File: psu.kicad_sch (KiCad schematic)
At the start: 9 parts, among them T1 Transformer_1P_2S, U2 PC817, U3 TL431DBZ

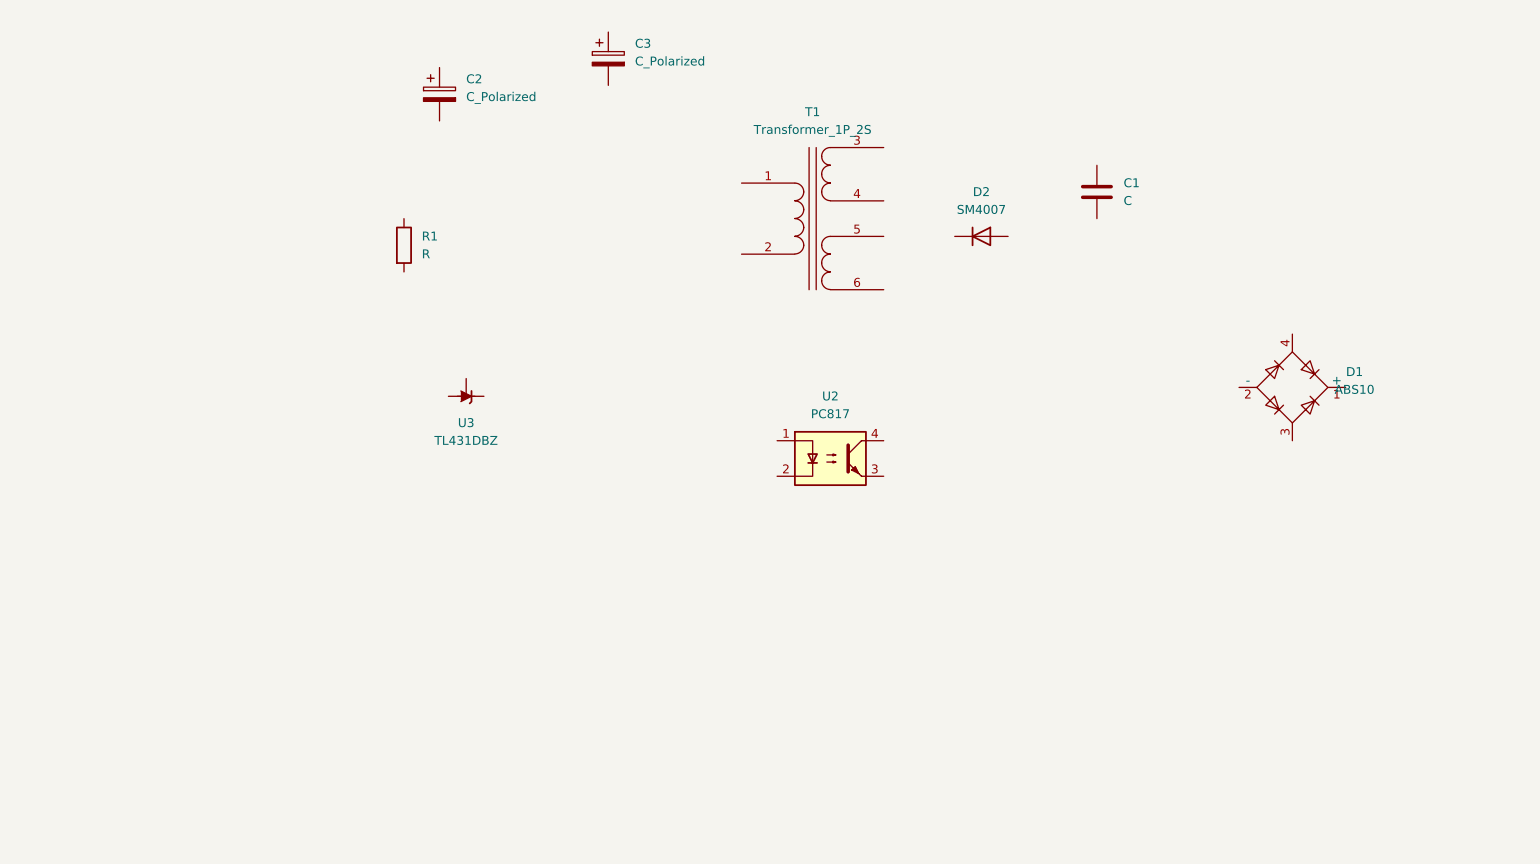
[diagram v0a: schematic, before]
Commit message: progress in psu section:footprints added:flyback ic yet to be added
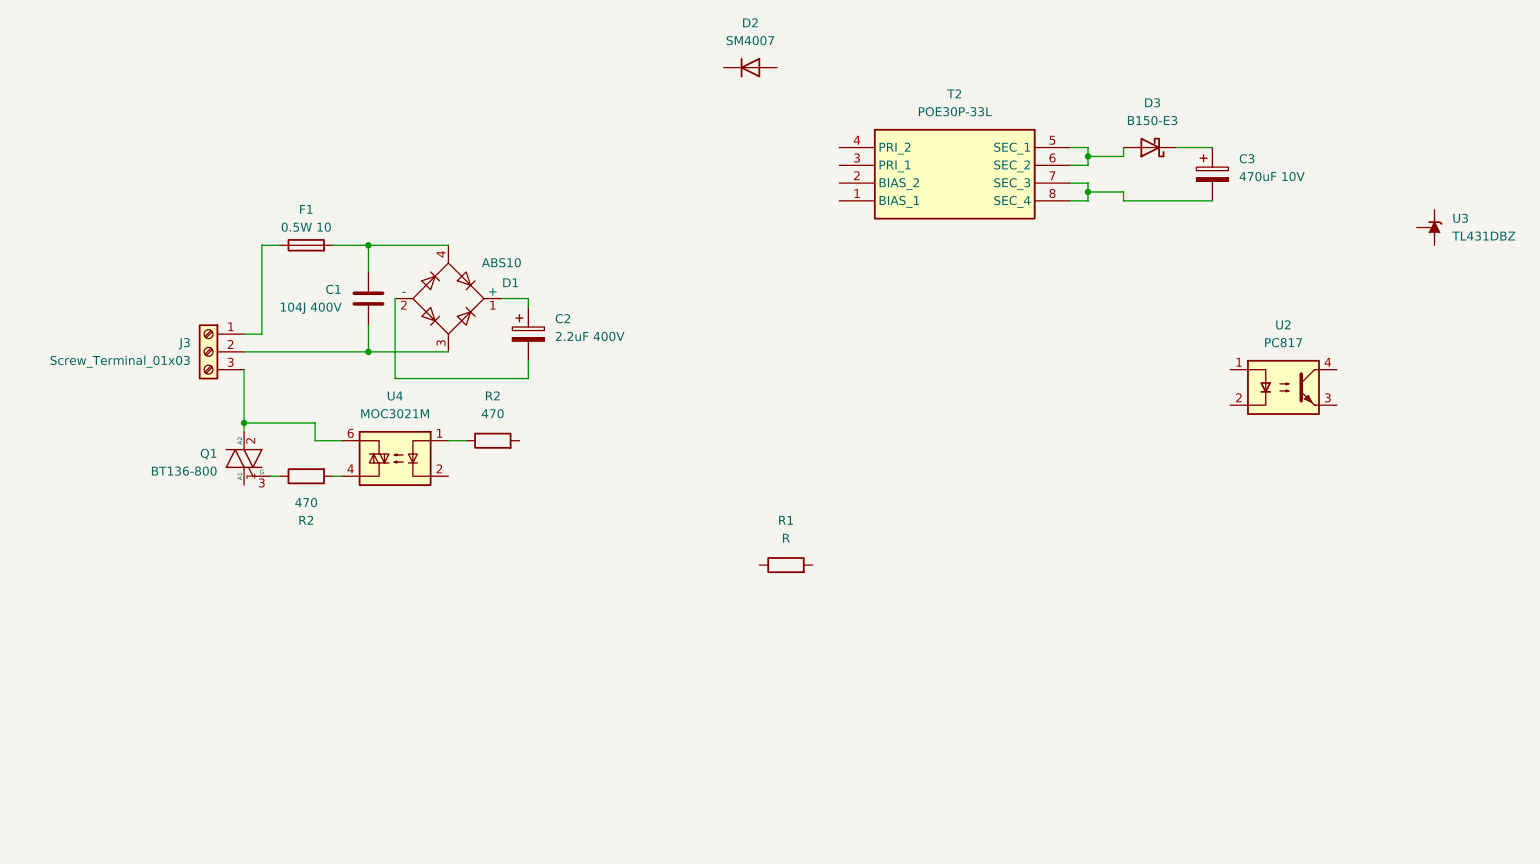
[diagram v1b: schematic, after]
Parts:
- removed T1: Transformer_1P_2S, symbol Device:Transformer_1P_2S
- added D3: B150-E3, Diode_SMD:D_SMA, symbol Diode:B150-E3
- added F1: 0.5W 10, Resistor_THT:R_Axial_DIN0411_L9.9mm_D3.6mm_P15.24mm_Horizontal, symbol Device:Fuse
- added J3: Screw_Terminal_01x03, TerminalBlock_Phoenix:TerminalBlock_Phoenix_MKDS-1,5-3-5.08_1x03_P5.08mm_Horizontal, symbol Connector:Screw_Terminal_01x03
- added Q1: BT136-800, Package_TO_SOT_THT:TO-220-3_Vertical, symbol Triac_Thyristor:BT136-800
- added R2 (x2): 470, Resistor_SMD:R_1206_3216Metric, symbol Device:R
- added T2: POE30P-33L, footprint:POE30P33L, symbol POE30P-33L:POE30P-33L
- added U4: MOC3021M, Package_DIP:DIP-6_W8.89mm_SMDSocket_LongPads, symbol Relay_SolidState:MOC3021M
- C1: value C -> 104J 400V; footprint (none) -> Capacitor_THT:C_Rect_L10.3mm_W4.5mm_P7.50mm_MKS4
- C2: value C_Polarized -> 2.2uF 400V; footprint (none) -> Capacitor_THT:CP_Radial_D8.0mm_P3.50mm
- C3: value C_Polarized -> 470uF 10V
- U2: footprint Package_DIP:DIP-4_W7.62mm -> Package_DIP:DIP-4_W7.62mm_SMDSocket_SmallPads
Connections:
- net at D1.1 (+): now also C2.1
- net at D1.2 (-): now also C2.2
- net at D1.3: now also C1.2, J3.2 (Pin_2)
- net at D1.4: now also C1.1, F1.2
- net at C3.1: now also D3.1 (K)
- net at C3.2: now also T2.7 (SEC_3), T2.8 (SEC_4)
- new net: D3.2 (A), T2.5 (SEC_1), T2.6 (SEC_2)
- new net: F1.1, J3.1 (Pin_1)
- new net: R2.1, U4.1
- new net: R2.2, U4.4
- new net: J3.3 (Pin_3), Q1.2 (A2), U4.6
- new net: Q1.3 (G), R2.1
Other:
- moved on the sheet: C1, C2, C3, D1, D2, R1, U2, U3

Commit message: viper22as, transformer, hierarchical connections
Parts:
- added U5: VIPer22AS, Package_SO:SOIC-8_3.9x4.9mm_P1.27mm, symbol Regulator_Switching:VIPer22AS
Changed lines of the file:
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@@
     (stroke (width 0) (type default))
+  )
+  (hierarchical_label "Gnd out" (shape output) (at 60.96 140.97 0) (fields_autoplaced)
+    (effects (font (size 1.27 1.27)) (justify left))
+  )
+  (hierarchical_label "TRIAC in" (shape input) (at 60.96 148.59 0) (fields_autoplaced)
+    (effects (font (size 1.27 1.27)) (justify left))
+  )
+  (hierarchical_label "3.3V out" (shape output) (at 60.96 134.62 0) (fields_autoplaced)
+    (effects (font (size 1.27 1.27)) (justify left))
+  )
+  (hierarchical_label "ZV signal out" (shape output) (at 60.96 154.94 0) (fields_autoplaced)
+    (effects (font (size 1.27 1.27)) (justify left))
+  )
+  (symbol (lib_id "Regulator_Switching:VIPer22AS") (at 171.45 135.89 0) (unit 1)
+    (in_bom yes) (on_board yes) (dnp no) (fields_autoplaced)
+    (property "Reference" "U5" (at 182.88 134.62 0)
+      (effects (font (size 1.27 1.27)) (justify left))
+    )
+    (property "Value" "VIPer22AS" (at 182.88 137.16 0)
+      (effects (font (size 1.27 1.27)) (justify left))
+    )
+    (property "Footprint" "Package_SO:SOIC-8_3.9x4.9mm_P1.27mm" (at 182.88 134.62 0)
+      (effects (font (size 1.27 1.27) italic) (justify left) hide)
+    )
+    (property "Datasheet" "http://www.st.com/web/en/resource/technical/document/datasheet/CD00087939.pdf" (at 171.45 135.89 0)
+      (effects (font (size 1.27 1.27)) hide)
+    )
+    (pin "1")
+    (pin "2")
+    (pin "3")
+    (pin "4")
+    (pin "5")
+    (pin "6")
+    (pin "7")
+    (pin "8")
+    (instances
+      (project "esp32-iot-socket"
+        (path "/45e1e5e5-a388-432c-8d2b-80b7f8345075/f2ceae1f-980b-462e-ad1f-32098829a58d"
+          (reference "U5") (unit 1)
+        )
+      )
+    )
   )
   (symbol (lib_id "Diode:B150-E3") (at 187.96 55.88 180) (unit 1)

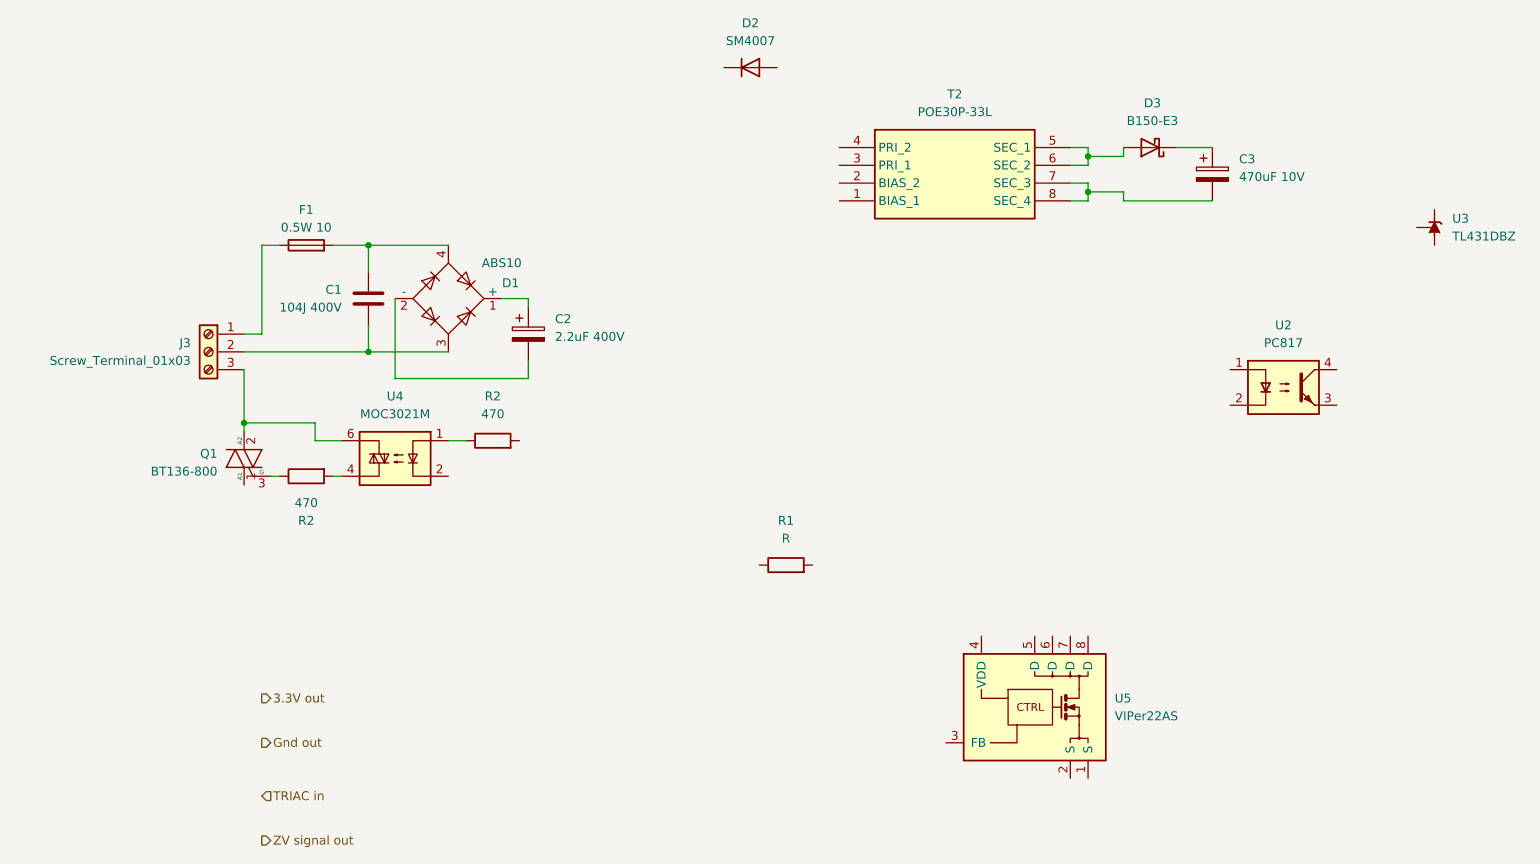
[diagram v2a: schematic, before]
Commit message: completed psu schematic sheet
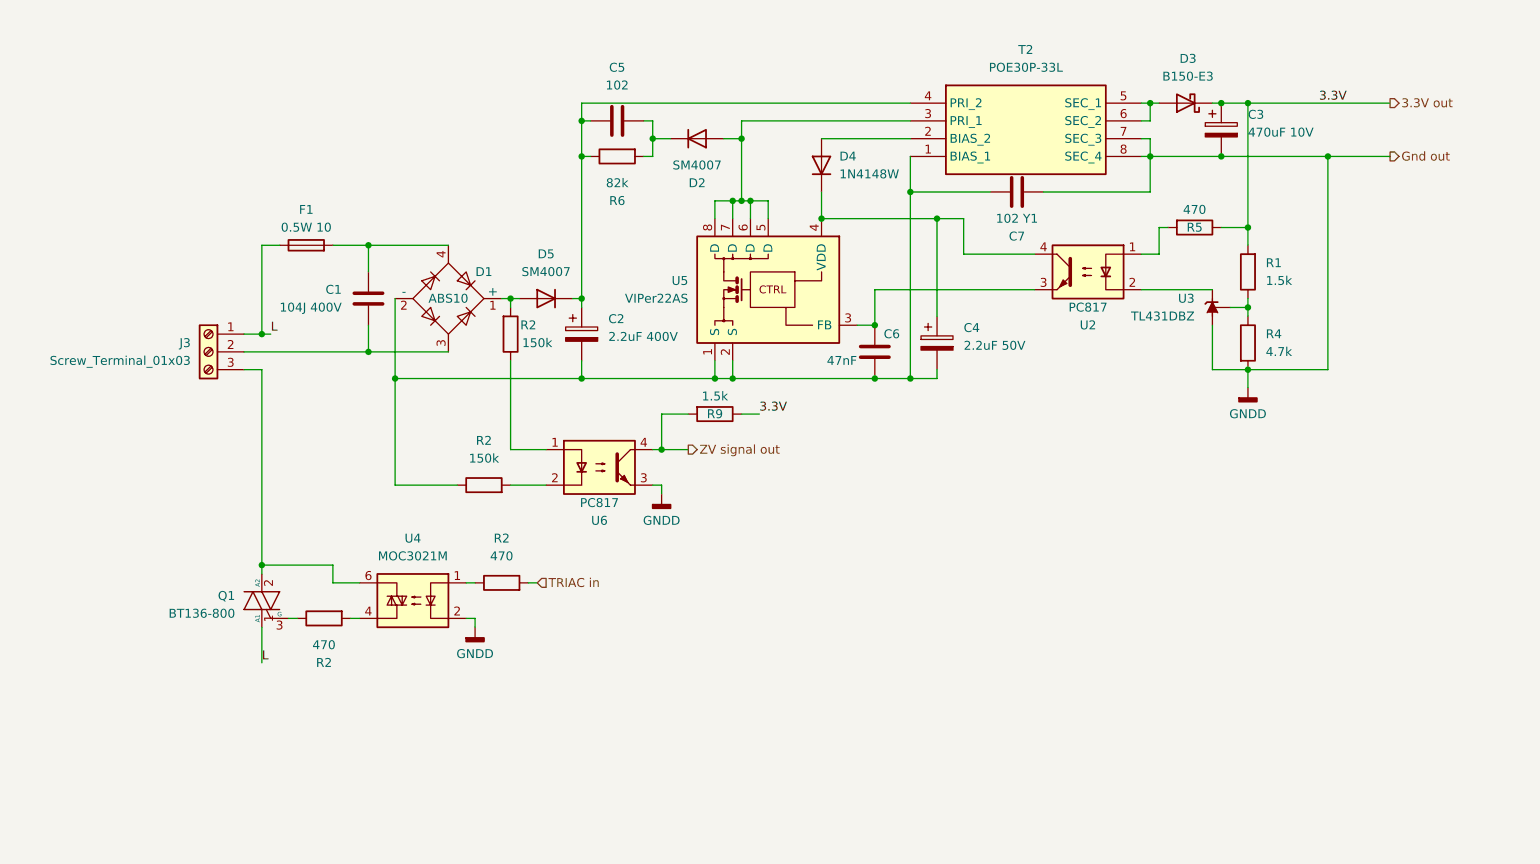
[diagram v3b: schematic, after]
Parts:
- added C4: 2.2uF 50V, Capacitor_THT:CP_Radial_D5.0mm_P2.50mm, symbol Device:C_Polarized
- added C5: 102, Capacitor_THT:C_Rect_L4.6mm_W2.0mm_P2.50mm_MKS02_FKP02, symbol Device:C
- added C6: 47nF, Capacitor_SMD:C_01005_0402Metric_Pad0.57x0.30mm_HandSolder, symbol Device:C
- added C7: 102 Y1, Capacitor_THT:C_Disc_D5.0mm_W2.5mm_P5.00mm, symbol Device:C
- added D4: 1N4148W, Diode_SMD:D_SOD-123, symbol Diode:1N4148W
- added D5: SM4007, Diode_SMD:D_MELF, symbol Diode:SM4007
- added R2 (x2): 150k, Resistor_SMD:R_1206_3216Metric, symbol Device:R
- added R4: 4.7k, Resistor_SMD:R_0402_1005Metric, symbol Device:R
- added R5: 470, Resistor_SMD:R_0402_1005Metric, symbol Device:R
- added R6: 82k, Resistor_SMD:R_1206_3216Metric_Pad1.30x1.75mm_HandSolder, symbol Device:R
- added R9: 1.5k, Resistor_SMD:R_0402_1005Metric, symbol Device:R
- added U6: PC817, Package_DIP:DIP-4_W7.62mm_SMDSocket_SmallPads, symbol Isolator:PC817
- C3: footprint (none) -> Capacitor_SMD:CP_Elec_5x5.3
- R1: value R -> 1.5k; footprint (none) -> Resistor_SMD:R_0402_1005Metric
- R2: footprint Resistor_SMD:R_1206_3216Metric -> Resistor_SMD:R_0402_1005Metric
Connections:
- net 3.3V out: now also C3.1, D3.1 (K), R1.2, R5.1, R9.1
- net TRIAC in: now also R2.2
- net ZV signal out: now also R9.2, U6.4
- net at U5.1 (S): now also C2.2, D1.2 (-), T2.1 (BIAS_1), U5.2 (S), C4.2, C6.2, C7.1, R2.1
- net at U5.3 (FB): now also U2.3, C6.1
- net at U5.4 (VDD): now also U2.4, C4.1, D4.1 (K)
- net at U5.5 (D): now also D2.2 (A), T2.3 (PRI_1), U5.6 (D), U5.7 (D), U5.8 (D)
- net at U3.1 (K): now also U2.2
- net at U3.2 (REF): now also R1.1, R4.1
- net GNDD: now reaches U3.3 (A)
- net GNDD: now also C3.2, T2.7 (SEC_3), T2.8 (SEC_4), U4.2, C7.2, R4.2, U6.3
- net at D2.1 (K): now also C5.2, R6.2
- net L: now reaches F1.1, J3.1 (Pin_1)
- net L: now also Q1.1 (A1)
- net at T2.2 (BIAS_2): now also D4.2 (A)
- net at T2.4 (PRI_2): now also C2.1, C5.1, D5.1 (K), R6.1
- net at D1.1 (+): now also D5.2 (A), R2.2; no longer C2.1
- net at U2.1: now also R5.2
- new net: R2.2, U6.2
- new net: R2.1, U6.1
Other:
- moved on the sheet: C2, C3, D2, D3, Q1, R1, R2, T2, U2, U3, U4, U5

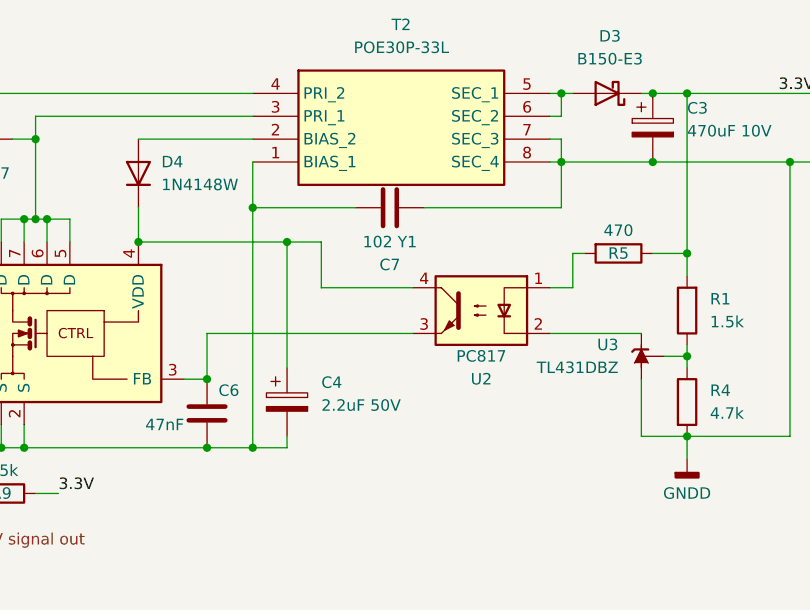
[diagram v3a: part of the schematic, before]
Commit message: added antenna symbol
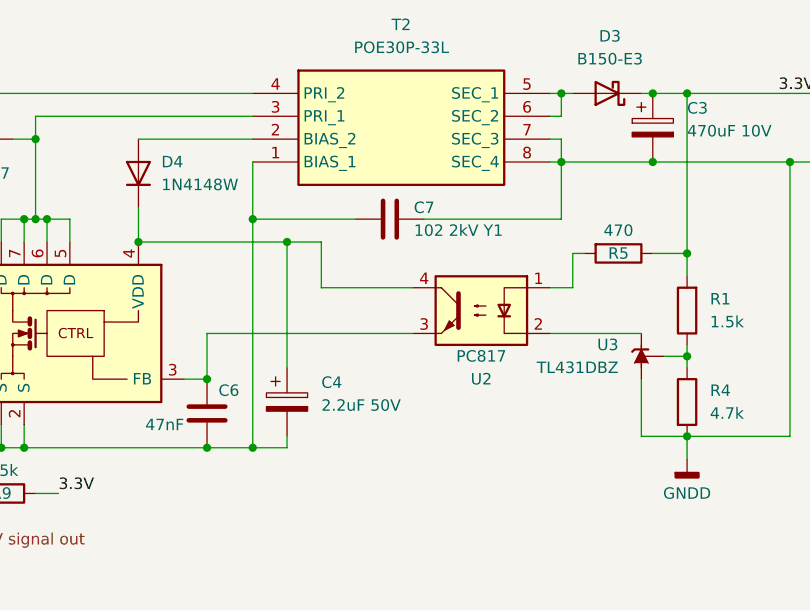
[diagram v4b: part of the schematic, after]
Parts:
- C7: value 102 Y1 -> 102 2kV Y1
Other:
- moved on the sheet: C7
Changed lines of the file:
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@@
   (junction (at 128.27 88.9) (diameter 0) (color 0 0 0 0)
   )
-  (junction (at 153.67 62.23) (diameter 0) (color 0 0 0 0)
-  )
   (junction (at 201.93 67.31) (diameter 0) (color 0 0 0 0)
   )
@@
   (junction (at 118.11 99.06) (diameter 0) (color 0 0 0 0)
   )
+  (junction (at 153.67 63.5) (diameter 0) (color 0 0 0 0)
+  )
   (junction (at 116.84 54.61) (diameter 0) (color 0 0 0 0)
   )
@@
     (stroke (width 0) (type default))
   )
-  (wire (pts (xy 172.72 62.23) (xy 187.96 62.23))
+  (wire (pts (xy 172.72 63.5) (xy 187.96 63.5))
     (stroke (width 0) (type default))
   )
@@
     (stroke (width 0) (type default))
   )
-  (wire (pts (xy 187.96 62.23) (xy 187.96 57.15))
+  (wire (pts (xy 187.96 63.5) (xy 187.96 57.15))
     (stroke (width 0) (type default))
   )
@@
     (stroke (width 0) (type default))
   )
-  (wire (pts (xy 153.67 62.23) (xy 165.1 62.23))
+  (wire (pts (xy 153.67 63.5) (xy 165.1 63.5))
     (stroke (width 0) (type default))
   )
@@
     (stroke (width 0) (type default))
   )
+  (wire (pts (xy 153.67 63.5) (xy 153.67 88.9))
+    (stroke (width 0) (type default))
+  )
   (wire (pts (xy 189.23 49.53) (xy 187.96 49.53))
     (stroke (width 0) (type default))
@@
     (stroke (width 0) (type default))
   )
-  (wire (pts (xy 153.67 57.15) (xy 153.67 62.23))
-    (stroke (width 0) (type default))
-  )
   (wire (pts (xy 198.12 49.53) (xy 201.93 49.53))
     (stroke (width 0) (type default))
@@
     (stroke (width 0) (type default))
   )
-  (wire (pts (xy 153.67 62.23) (xy 153.67 88.9))
+  (wire (pts (xy 153.67 57.15) (xy 153.67 63.5))
     (stroke (width 0) (type default))
   )
@@
     )
   )
-  (symbol (lib_id "Device:C") (at 168.91 62.23 90) (unit 1)
+  (symbol (lib_id "Device:C") (at 168.91 63.5 90) (unit 1)
     (in_bom yes) (on_board yes) (dnp no)
-    (property "Reference" "C7" (at 168.91 68.58 90)
-      (effects (font (size 1.27 1.27)))
-    )
-    (property "Value" "102 Y1" (at 168.91 66.04 90)
-      (effects (font (size 1.27 1.27)))
-    )
-    (property "Footprint" "Capacitor_THT:C_Disc_D5.0mm_W2.5mm_P5.00mm" (at 172.72 61.2648 0)
-      (effects (font (size 1.27 1.27)) hide)
-    )
-    (property "Datasheet" "~" (at 168.91 62.23 0)
-      (effects (font (size 1.27 1.27)) hide)
-    )
+    (property "Reference" "C7" (at 172.72 62.23 90)
+      (effects (font (size 1.27 1.27)))
+    )
+    (property "Value" "102 2kV Y1" (at 176.53 64.77 90)
+      (effects (font (size 1.27 1.27)))
+    )
+    (property "Footprint" "Capacitor_THT:C_Disc_D5.0mm_W2.5mm_P5.00mm" (at 172.72 62.5348 0)
+      (effects (font (size 1.27 1.27)) hide)
+    )
+    (property "Datasheet" "~" (at 168.91 63.5 0)
+      (effects (font (size 1.27 1.27)) hide)
+    )
